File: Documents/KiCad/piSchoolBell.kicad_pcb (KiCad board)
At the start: 2 copper layers, 64.1 x 67.9 mm, 16 parts, among them J1 ZS-042_4-pin_RTC_Module, J2 10-pin_header_LCD_interface, J3 Raspberry_Pi_2_3_all_pin_orde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, J4 3-pin_KY-019_relay_header, J5 2-pin_NO_switch_header, J6 2-pin_NO_switch_header, J7 2-pin_NO_switch_header, J8 2-pin_NO_switch_header

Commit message: kicad
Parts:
- added D1: LED, My_Misc:LED_D5.0mm_larger_pads, F.Cu at (132.7, 126.4)
- added R9: 220R, My_Misc:R_Axial_DIN0207_L6.3mm_D2.5mm_P10.16mm_Horizontal_larger_pads, F.Cu at (127.0, 126.4)
- moved J4 29.5 mm to (141.0, 126.4), turned to 90 degrees
- moved R1 18.1 mm to (134.6, 89.5)
- moved R2 17.9 mm to (128.9, 89.5)
- moved R3 17.8 mm to (123.2, 89.5)
- moved R4 17.8 mm to (117.5, 89.5)
- moved J5 15.4 mm to (134.6, 100.3)
- moved J6 15.4 mm to (127.0, 100.3)
- moved J7 15.4 mm to (119.4, 100.3)
- moved R5 13.5 mm to (134.6, 115.6)
- moved R6 13.5 mm to (127.0, 115.6)
- moved R7 13.5 mm to (119.4, 115.6)
- moved R8 4.62 mm to (111.1, 115.6)
- moved J8 3.81 mm to (111.1, 100.3), turned to 180 degrees
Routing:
- net Net-(J3-Pad1): track 46.2 -> 105.2 mm, vias 9 -> 2
- net Net-(D1-Pad2): track 62.7 -> 95.1 mm
- net Net-(J1-Pad3): track 74.3 -> 44.8 mm
- net Net-(J3-Pad12): track 71.7 -> 52.5 mm
- net Net-(J3-Pad16): track 82.1 -> 67.0 mm
- net Net-(J3-Pad18): track 90.7 -> 79.1 mm
- net Net-(J8-Pad2): track 12.5 -> 21.8 mm
- net Net-(J3-Pad22): track 101.9 -> 92.6 mm
- net Net-(J1-Pad4): track 114.5 -> 123.5 mm
- net Net-(D1-Pad1): track 0.00 -> 5.72 mm
- net Net-(J6-Pad2): track 15.1 -> 20.0 mm
- net Net-(J5-Pad2): track 14.9 -> 19.2 mm
- net Net-(J7-Pad2): track 16.5 -> 20.8 mm
- net Net-(J2-Pad3): track 19.3 -> 20.8 mm
- net Net-(J1-Pad2): track 22.9 -> 21.8 mm
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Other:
- board size 64.1 x 67.9 mm -> 63.5 x 67.3 mm

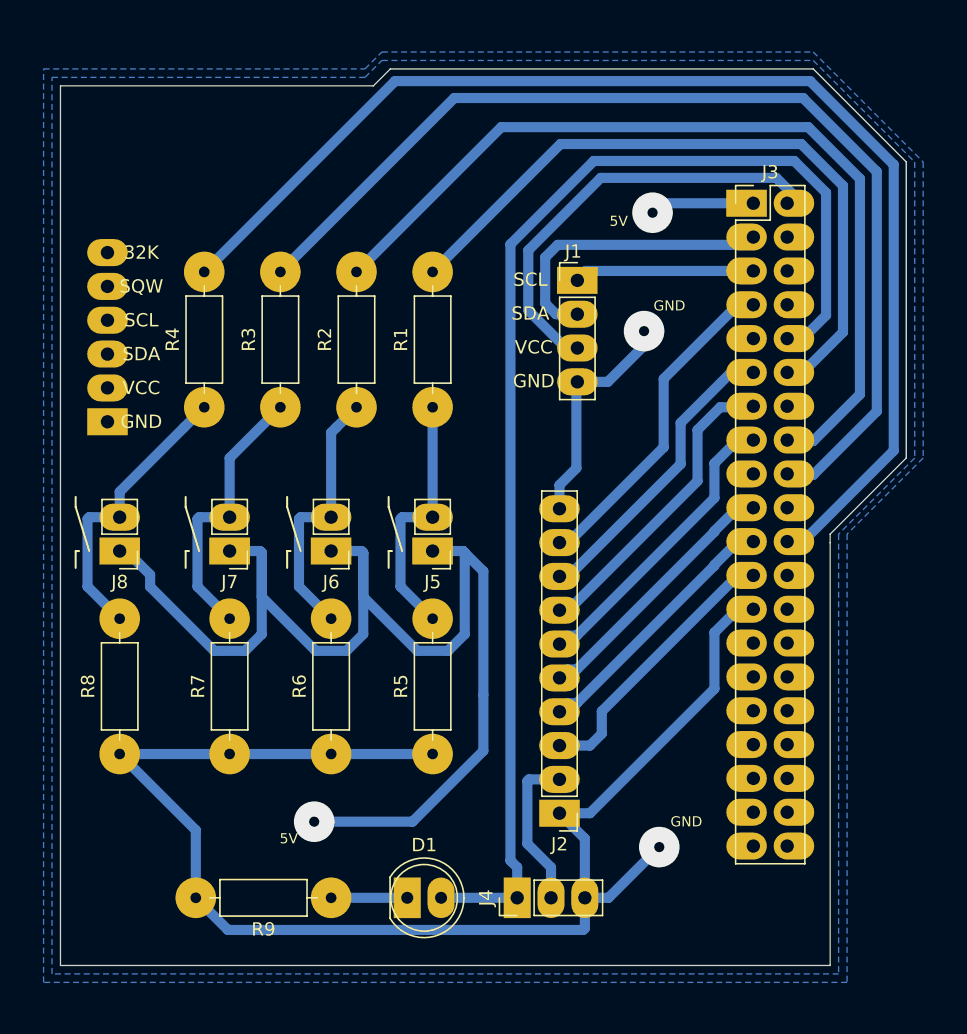
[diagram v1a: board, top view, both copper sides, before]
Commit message: moved pin for backlight in KiCad
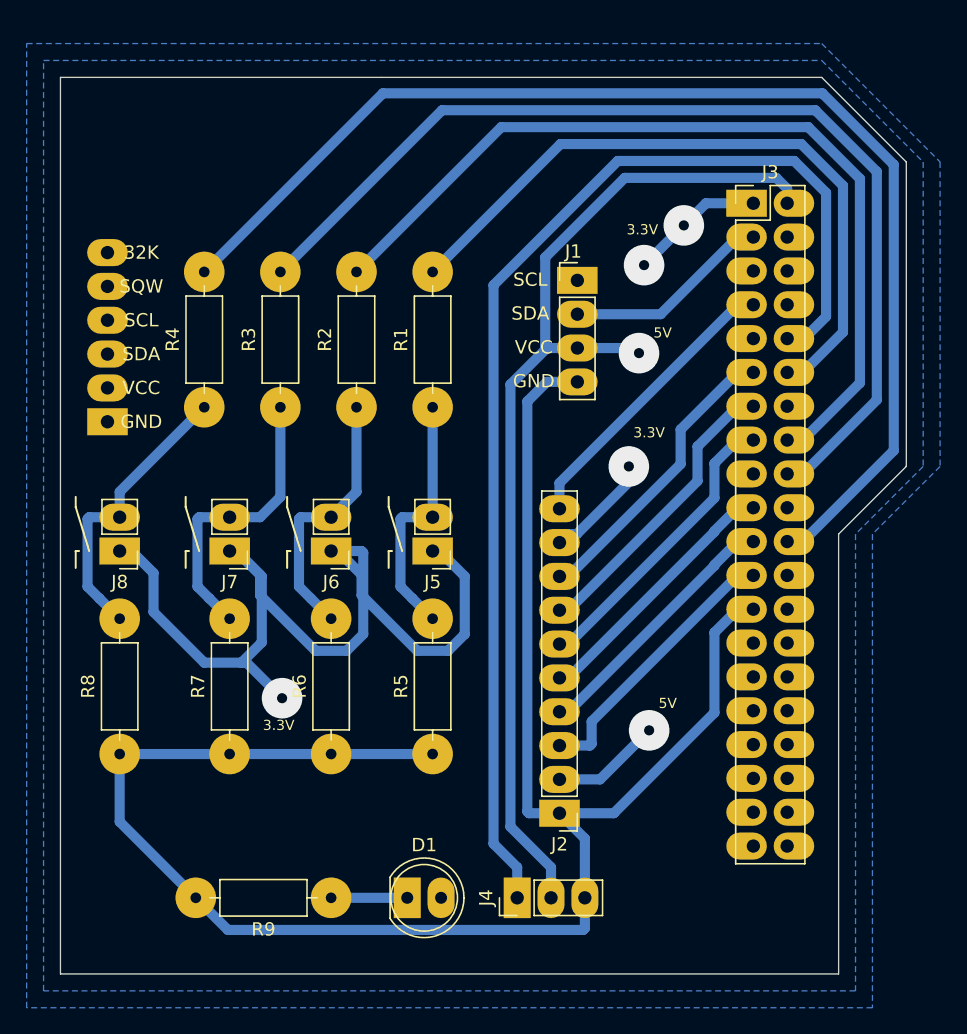
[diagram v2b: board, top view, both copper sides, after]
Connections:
- J2 pad 10: Net-(J1-Pad4) -> Net-(J2-Pad10)
- J3 pad 1: Net-(J3-Pad1) -> Net-(J2-Pad9)
- J3 pad 7: Net-(J2-Pad9) -> Net-(J2-Pad10)
- J5 pad 1: Net-(J3-Pad1) -> Net-(J2-Pad9)
- J6 pad 1: Net-(J3-Pad1) -> Net-(J2-Pad9)
- J7 pad 1: Net-(J3-Pad1) -> Net-(J2-Pad9)
- J8 pad 1: Net-(J3-Pad1) -> Net-(J2-Pad9)
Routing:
- net Net-(J3-Pad1): track 105.2 -> 0.00 mm, vias 2 -> 0
- net Net-(J2-Pad9): track 24.3 -> 91.9 mm, vias 0 -> 4
- net Net-(J1-Pad3): track 44.8 -> 88.3 mm, vias 0 -> 2
- net Net-(J2-Pad10): track 0.00 -> 22.0 mm
- net Net-(J1-Pad4): track 123.5 -> 138.4 mm, vias 2 -> 0
- net Net-(J1-Pad1): track 13.6 -> 0.00 mm
- net Net-(J1-Pad2): track 21.8 -> 15.6 mm
- net Net-(D1-Pad2): track 95.1 -> 89.5 mm
- net Net-(J7-Pad2): track 20.8 -> 22.1 mm
- net Net-(J3-Pad18): track 79.1 -> 77.9 mm
- net Net-(J3-Pad22): track 92.6 -> 91.8 mm
- net Net-(J2-Pad6): track 21.8 -> 22.4 mm
- net Net-(J2-Pad4): track 19.3 -> 19.9 mm
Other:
- outline, holes or cut-outs redrawn
- board text added: "3.3V"
- board text removed: "GND"
